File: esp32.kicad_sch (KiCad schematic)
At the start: 51 parts, among them J4 Connector-12x1, J5 Conn_01x04, J6 TC2030-IDC, J8 USB_C_Receptacle_USB2.0, Q1 2N7002K, SW1 SWITCH-SPST, SW2 SWITCH-SPST, U5 SN74AVC4T774, U6 ESP32-S3-WROOM-1, Y1 32.768kHz

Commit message: move fan connector, create new buttons
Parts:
- SW1, SW2: footprint bitaxe:EVQ9P701P-switch -> bitaxe:TL3330-switch; DK P19095CT-ND -> EG4389CT-ND; PARTNO EVQ-9P701P -> TL3330AF260QG
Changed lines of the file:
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@@
       (effects (font (size 1.27 1.27)) hide)
     )
-    (property "Footprint" "bitaxe:EVQ9P701P-switch" (at 51.435 57.15 0)
-      (effects (font (size 1.27 1.27)) hide)
-    )
-    (property "Datasheet" "https://api.pim.na.industrial.panasonic.com/file_stream/main/fileversion/245500" (at 51.435 59.69 0)
-      (effects (font (size 1.27 1.27)) hide)
-    )
-    (property "PARTNO" "EVQ-9P701P" (at 51.435 53.34 0)
-      (effects (font (size 1.27 1.27)) hide)
-    )
-    (property "DK" "P19095CT-ND" (at 51.435 50.8 0)
+    (property "Footprint" "bitaxe:TL3330-switch" (at 51.435 57.15 0)
+      (effects (font (size 1.27 1.27)) hide)
+    )
+    (property "Datasheet" "https://sten-eswitch-13110800-production.s3.amazonaws.com/system/asset/product_line/data_sheet/163/TL3330.pdf" (at 51.435 59.69 0)
+      (effects (font (size 1.27 1.27)) hide)
+    )
+    (property "PARTNO" "TL3330AF260QG" (at 51.435 53.34 0)
+      (effects (font (size 1.27 1.27)) hide)
+    )
+    (property "DK" "EG4389CT-ND" (at 51.435 50.8 0)
       (effects (font (size 1.27 1.27)) hide)
     )
@@
       (effects (font (size 1.27 1.27)) hide)
     )
-    (property "Footprint" "bitaxe:EVQ9P701P-switch" (at 21.59 67.31 0)
-      (effects (font (size 1.27 1.27)) hide)
-    )
-    (property "Datasheet" "https://api.pim.na.industrial.panasonic.com/file_stream/main/fileversion/245500" (at 21.59 69.85 0)
-      (effects (font (size 1.27 1.27)) hide)
-    )
-    (property "PARTNO" "EVQ-9P701P" (at 21.59 63.5 0)
-      (effects (font (size 1.27 1.27)) hide)
-    )
-    (property "DK" "P19095CT-ND" (at 21.59 60.96 0)
-      (effects (font (size 1.27 1.27)) hide)
-    )
+    (property "Footprint" "bitaxe:TL3330-switch" (at 21.59 67.31 0)
+      (effects (font (size 1.27 1.27)) hide)
+    )
+    (property "Datasheet" "https://sten-eswitch-13110800-production.s3.amazonaws.com/system/asset/product_line/data_sheet/163/TL3330.pdf" (at 21.59 69.85 0)
+      (effects (font (size 1.27 1.27)) hide)
+    )
+    (property "PARTNO" "TL3330AF260QG" (at 21.59 63.5 0)
+      (effects (font (size 1.27 1.27)) hide)
+    )
+    (property "DK" "EG4389CT-ND" (at 21.59 60.96 0)
+      (effects (font (size 1.27 1.27)) hide)
+    )

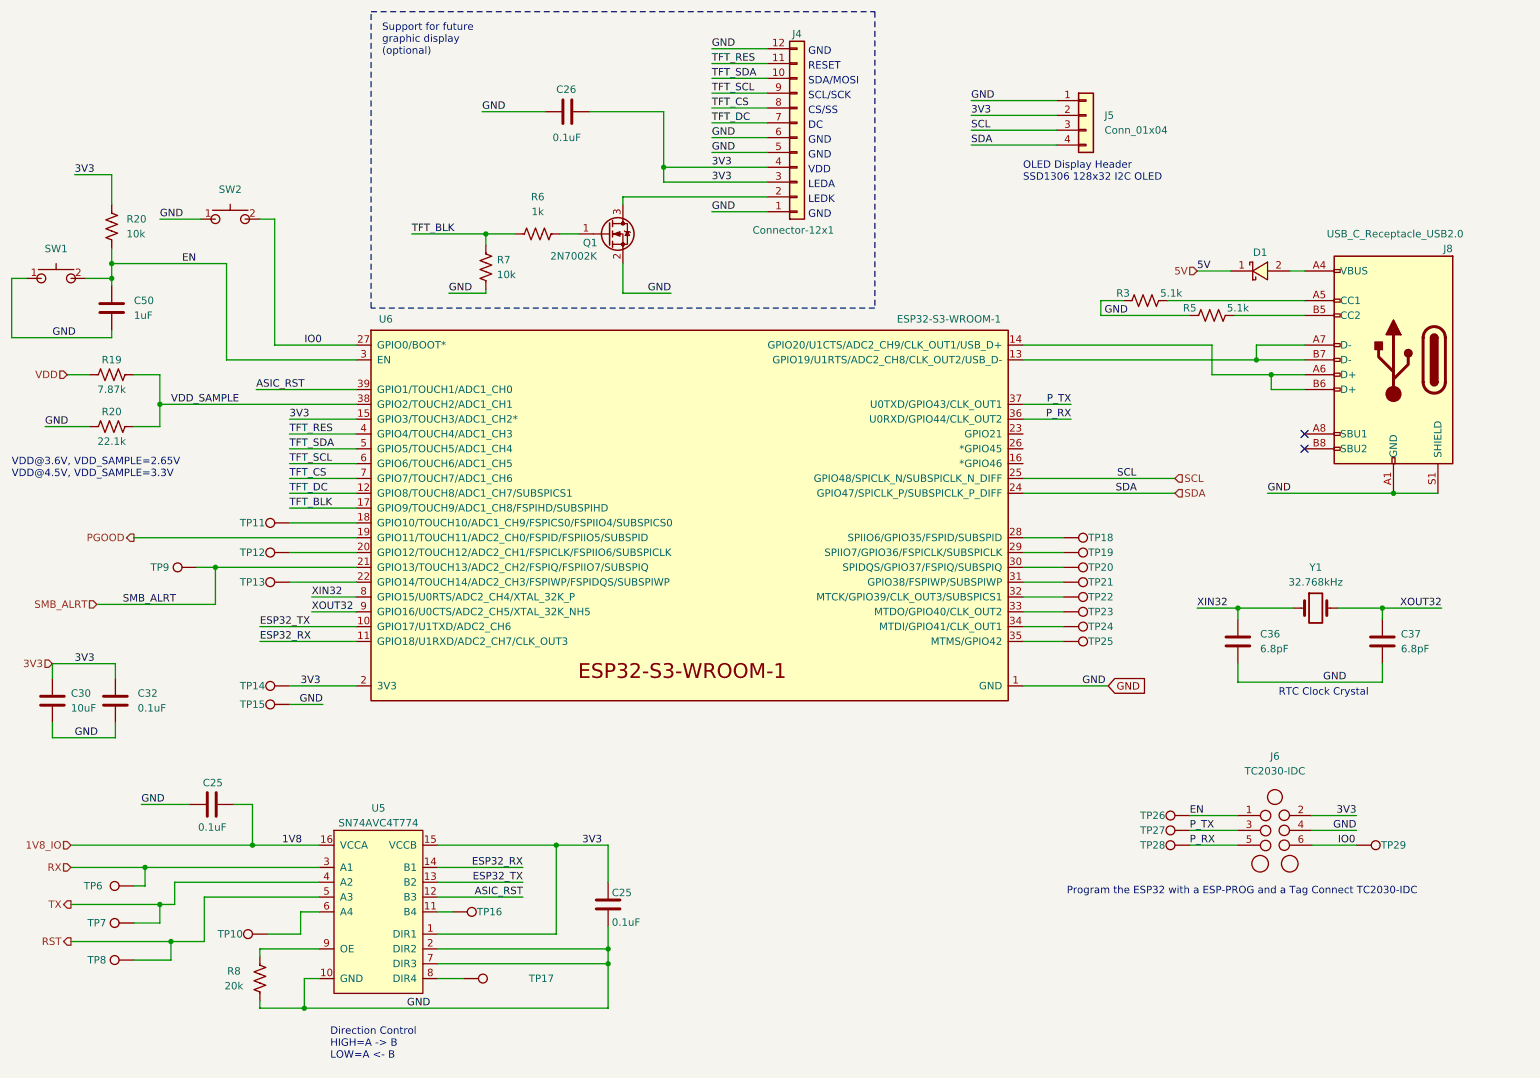
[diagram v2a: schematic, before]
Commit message: update to KiCad8, DNP 32KHz crystal, update BOM
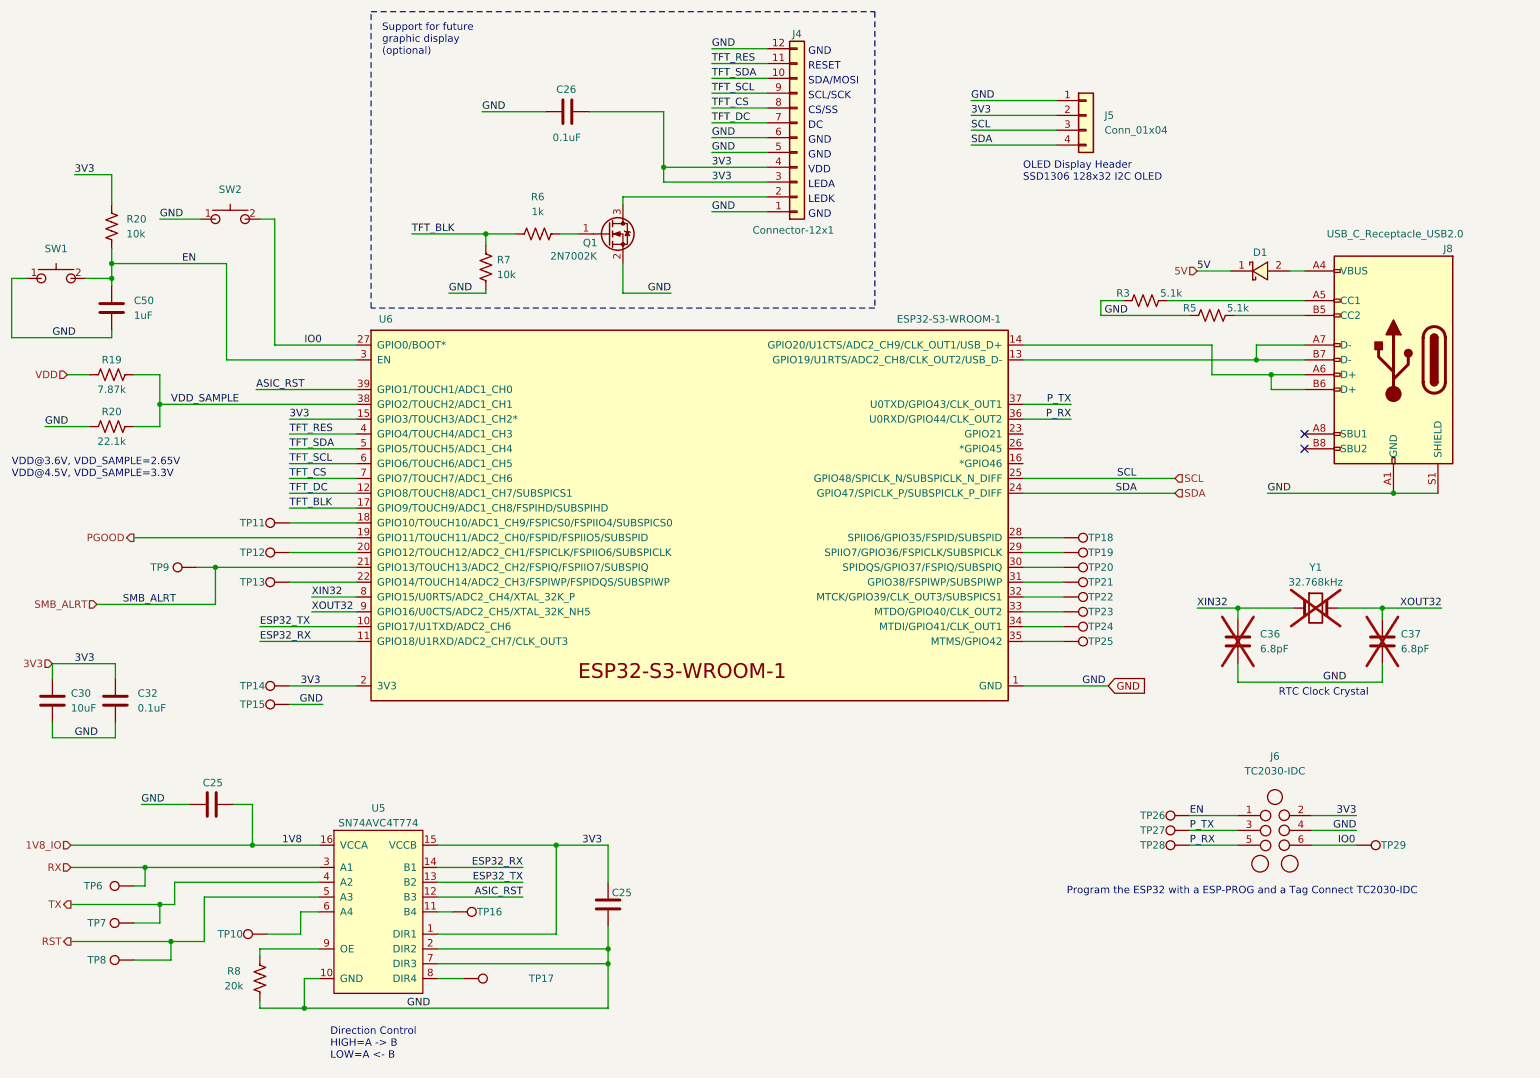
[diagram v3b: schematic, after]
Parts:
- C36, C37, Y1: now not fitted; now left out of the parts list

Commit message: change buttons to some that are easier to push
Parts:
- SW1, SW2: footprint bitaxe:TL3330-switch -> bitaxe:TL3340-switch; DK EG4389CT-ND -> EG4627CT-ND; PARTNO TL3330AF260QG -> TL3340AF160QG
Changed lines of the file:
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@@
 			)
 		)
-		(property "Footprint" "bitaxe:TL3330-switch"
+		(property "Footprint" "bitaxe:TL3340-switch"
 			(at 51.435 57.15 0)
 			(effects
@@
 			)
 		)
-		(property "Datasheet" "https://sten-eswitch-13110800-production.s3.amazonaws.com/system/asset/product_line/data_sheet/163/TL3330.pdf"
+		(property "Datasheet" "https://sten-eswitch-13110800-production.s3.amazonaws.com/system/asset/product_line/data_sheet/164/TL3340.pdf"
 			(at 51.435 59.69 0)
 			(effects
@@
 			)
 		)
-		(property "PARTNO" "TL3330AF260QG"
+		(property "PARTNO" "TL3340AF160QG"
 			(at 51.435 53.34 0)
 			(effects
@@
 			)
 		)
-		(property "DK" "EG4389CT-ND"
+		(property "DK" "EG4627CT-ND"
 			(at 51.435 50.8 0)
 			(effects
@@
 			)
 		)
-		(property "Footprint" "bitaxe:TL3330-switch"
+		(property "Footprint" "bitaxe:TL3340-switch"
 			(at 21.59 67.31 0)
 			(effects
@@
 			)
 		)
-		(property "Datasheet" "https://sten-eswitch-13110800-production.s3.amazonaws.com/system/asset/product_line/data_sheet/163/TL3330.pdf"
+		(property "Datasheet" "https://sten-eswitch-13110800-production.s3.amazonaws.com/system/asset/product_line/data_sheet/164/TL3340.pdf"
 			(at 21.59 69.85 0)
 			(effects
@@
 			)
 		)
-		(property "PARTNO" "TL3330AF260QG"
+		(property "PARTNO" "TL3340AF160QG"
 			(at 21.59 63.5 0)
 			(effects
@@
 			)
 		)
-		(property "DK" "EG4389CT-ND"
+		(property "DK" "EG4627CT-ND"
 			(at 21.59 60.96 0)
 			(effects

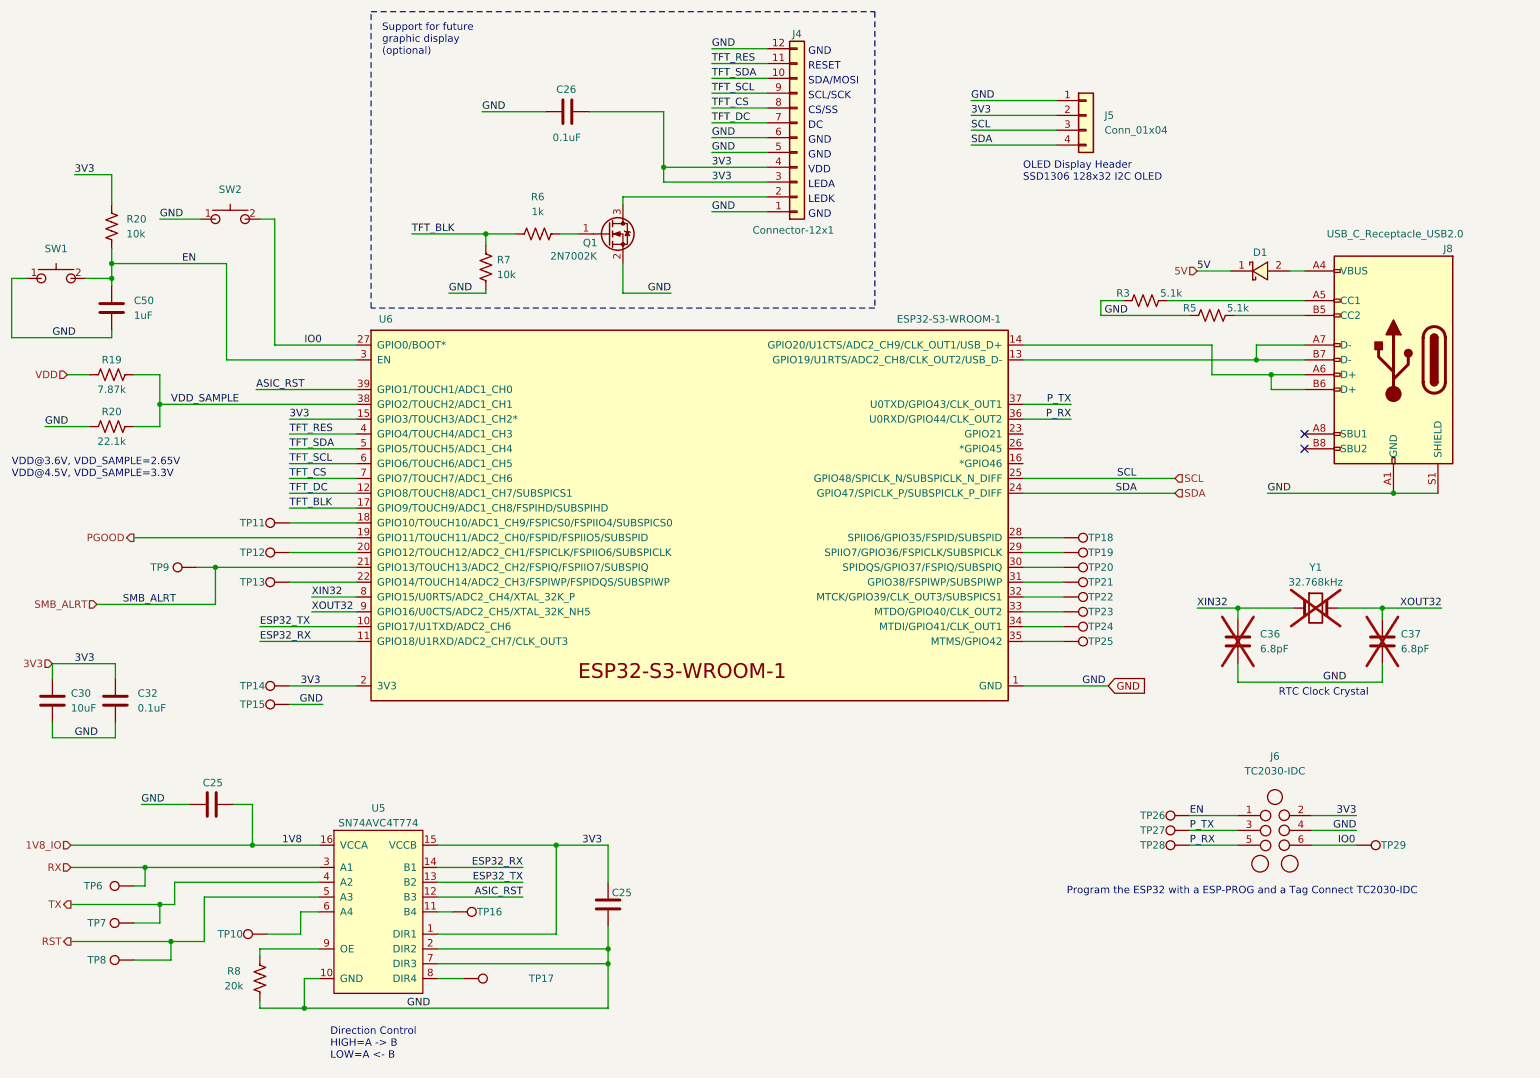
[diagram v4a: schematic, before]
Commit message: remove old display connector and add BAP, remove USB 5V supply, cleanup routing
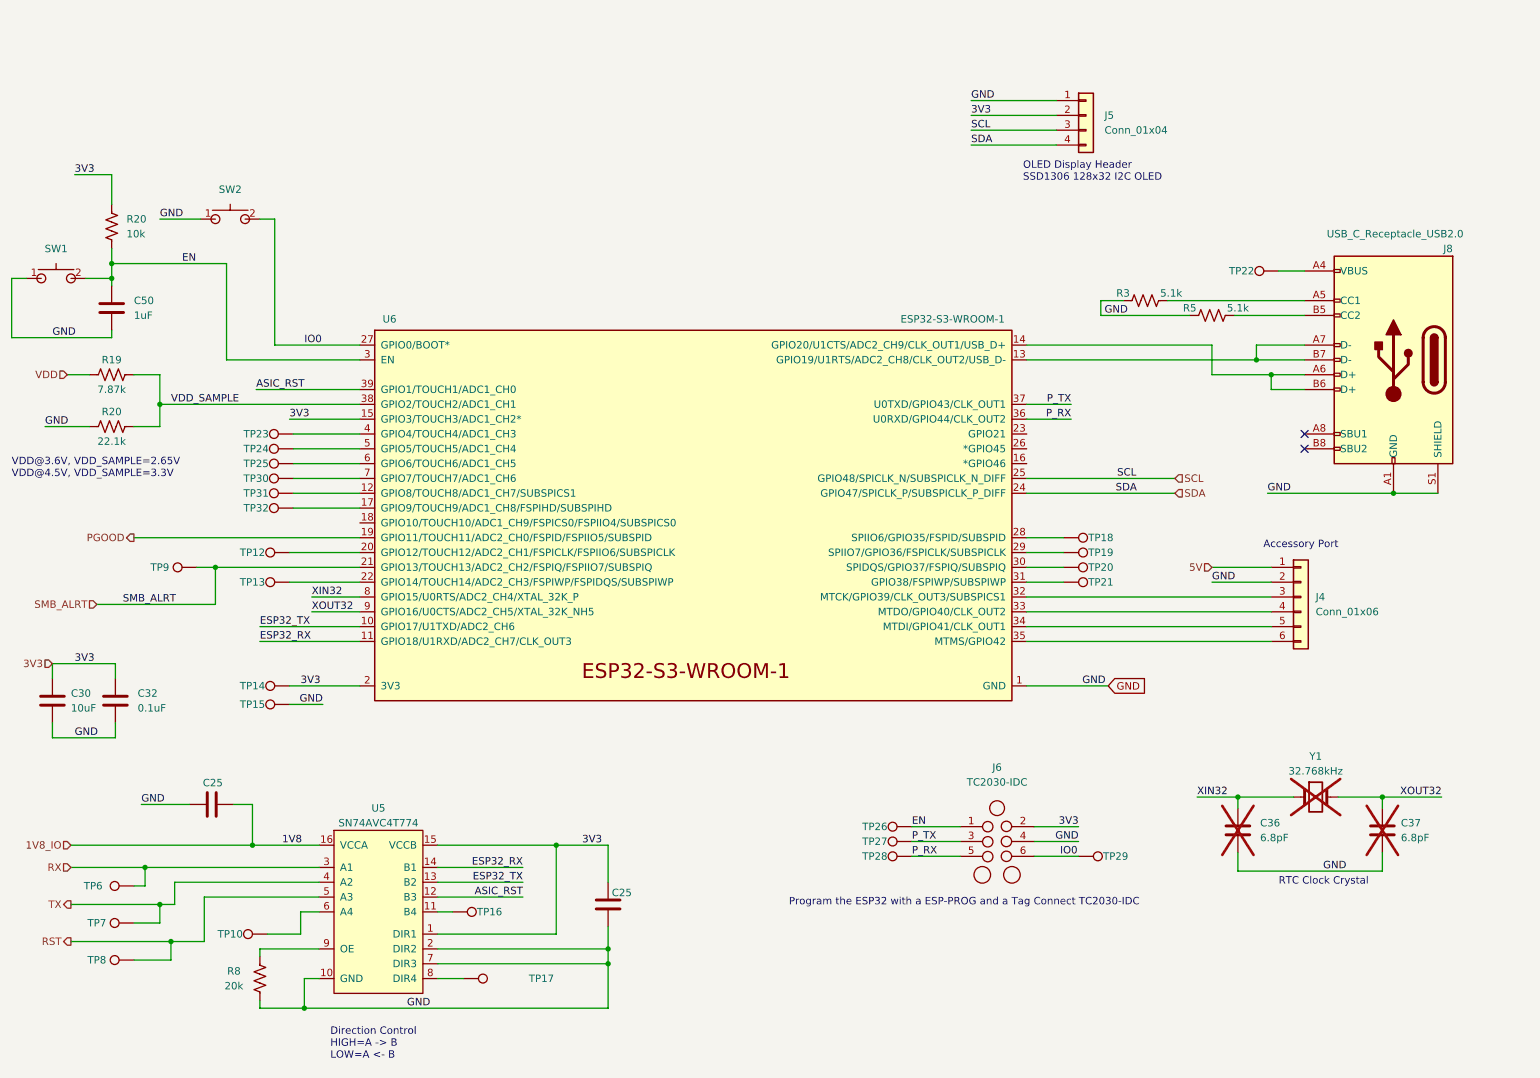
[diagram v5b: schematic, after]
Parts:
- removed C26: 0.1uF, Capacitor_SMD:C_0402_1005Metric, symbol Device:C
- removed D1: SS310, Diode_SMD:D_SMA, symbol lcsc:SS310_C85658
- removed J4: Connector-12x1, bitaxe:JST_GH_BM12B-GHS-TBT_1x12-1MP_P1.25mm_Vertical, symbol bitaxe:Conn_01x12
- removed Q1: 2N7002K, Package_TO_SOT_SMD:SOT-323_SC-70, symbol Transistor_FET:2N7002K
- removed R6: 1k, Resistor_SMD:R_0402_1005Metric, symbol Device:R_US
- removed R7: 10k, Resistor_SMD:R_0402_1005Metric, symbol Device:R_US
- removed TP11: TestPoint, TestPoint:TestPoint_Pad_D1.0mm, symbol Connector:TestPoint
- added J4: Conn_01x06, Connector_PinHeader_2.54mm:PinHeader_1x06_P2.54mm_Vertical, symbol Connector_Generic:Conn_01x06
- added TP30, TP31, TP32: TestPoint, TestPoint:TestPoint_Pad_D1.0mm, symbol Connector:TestPoint
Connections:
- net TFT_RES is gone; now on an unnamed net: U6.4 (GPIO4/TOUCH4/ADC1_CH3)
- net TFT_SDA is gone; now on an unnamed net: U6.5 (GPIO5/TOUCH5/ADC1_CH4)
- net 5V: now also J4.1 (Pin_1)
- net GND: now also J4.2 (Pin_2)
- net at J8.A4 (VBUS), J8.A9 (VBUS), J8.B4 (VBUS)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: now also TP22.1
- net at U6.35 (MTMS/GPIO42): now also J4.6 (Pin_6); no longer TP25.1
- net at U6.32 (MTCK/GPIO39/CLK_OUT3/SUBSPICS1): now also J4.3 (Pin_3); no longer TP22.1
- net at TP23.1: no longer U6.33 (MTDO/GPIO40/CLK_OUT2)
- net at TP24.1: no longer U6.34 (MTDI/GPIO41/CLK_OUT1)
- net TFT_BLK: no longer names the net of U6.17 (GPIO9/TOUCH9/ADC1_CH8/FSPIHD/SUBSPIHD)
- net TFT_BLK: now also TP32.1
- net TFT_CS: no longer names the net of U6.7 (GPIO7/TOUCH7/ADC1_CH6)
- net TFT_CS: now also TP30.1
- net TFT_DC: no longer names the net of U6.12 (GPIO8/TOUCH8/ADC1_CH7/SUBSPICS1)
- net TFT_DC: now also TP31.1
- net TFT_SCL: no longer names the net of U6.6 (GPIO6/TOUCH6/ADC1_CH5)
- net TFT_SCL: now also TP25.1
- new net: J4.4 (Pin_4), U6.33 (MTDO/GPIO40/CLK_OUT2)
- new net: J4.5 (Pin_5), U6.34 (MTDI/GPIO41/CLK_OUT1)
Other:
- note added: "Accessory Port"
- note removed: "CS/SS"
- note removed: "DC"
- note removed: "GND"
- note removed: "LEDA"
- note removed: "LEDK"
- note removed: "RESET"
- note removed: "SCL/SCK"
- note removed: "SDA/MOSI"
- note removed: "Support for future graphic display (optional)"
- note removed: "VDD"
- moved on the sheet: C36, C37, J6, TP26, TP27, TP28, TP29, U6, Y1

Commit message: generate BOM and gerber files for v303
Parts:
- renumbered C30 to C31, C32 to C33, J6 to J4, J4 to J6, TP9 to TP10, TP10 to TP11, TP23 to TP12, TP24 to TP13, TP25 to TP14, TP30 to TP15, TP31 to TP16, TP32 to TP17, TP12 to TP18, TP13 to TP19, TP14 to TP20, TP15 to TP21, TP16 to TP22, TP17 to TP23, TP26 to TP24, TP27 to TP25, TP28 to TP26, TP18 to TP27, TP19 to TP28, TP20 to TP29, TP21 to TP30, TP29 to TP31, TP22 to TP32, TP6 to TP7, TP7 to TP8, TP8 to TP9
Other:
- moved on the sheet: C25, C31, C36, C37, C50, J8, R19, R20, R8, SW2, TP11, TP18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

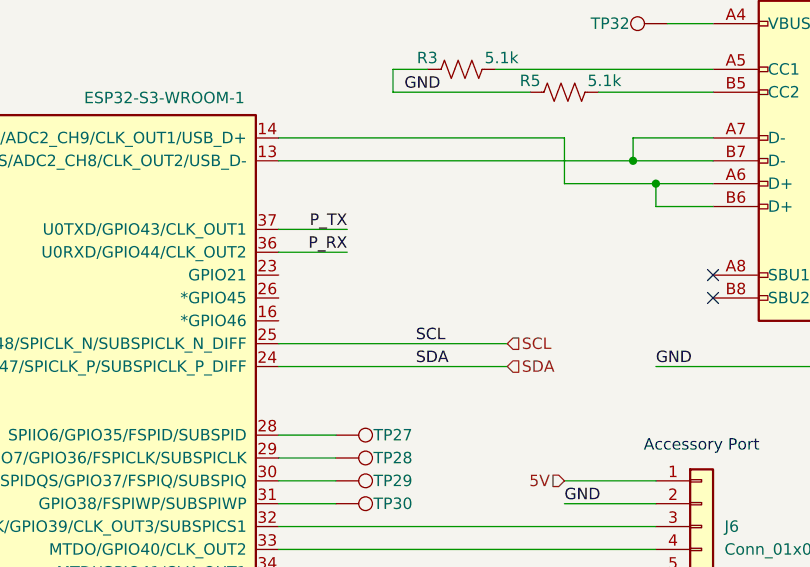
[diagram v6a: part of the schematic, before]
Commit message: swap out electrolytic output capacitor, add XT30 power connector
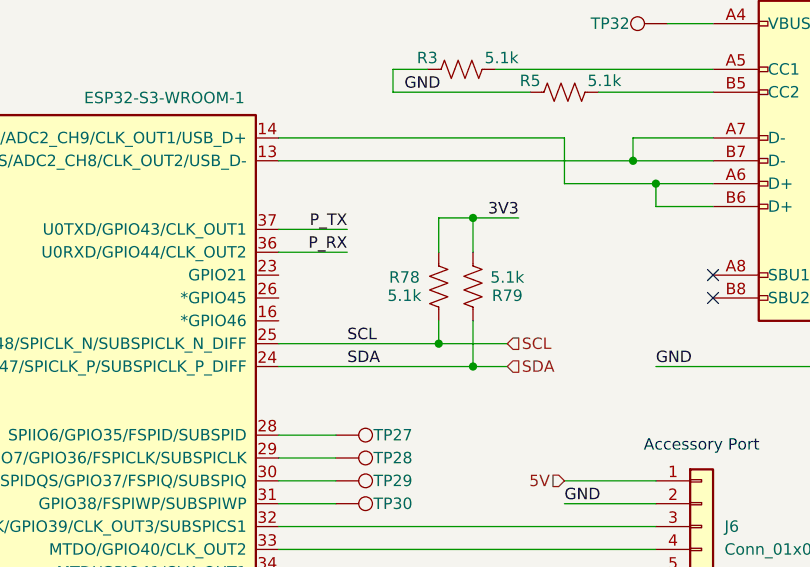
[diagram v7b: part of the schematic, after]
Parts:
- added R78, R79: 5.1k, Resistor_SMD:R_0402_1005Metric, symbol Device:R_US
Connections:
- net 3V3: now also R78.2, R79.1
- net SCL: now also R78.1
- net SDA: now also R79.2
